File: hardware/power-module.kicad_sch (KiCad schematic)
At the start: 35 parts, among them CN1 WJ2EDGRC-5.08-2P, K1 SRD-03VDC-SL-C, K2 SRD-03VDC-SL-C, K3 SRD-03VDC-SL-C, K4 SRD-03VDC-SL-C, Q1 BC547C, Q2 BC547C, U1 MIC5205-3.3YM5-MS, U2 PM254-2-05-W-8.5, U3 CC6903SO-10A, U4 ESP32-C3-MINI-1, U5 XC6206P332MR_C5148692

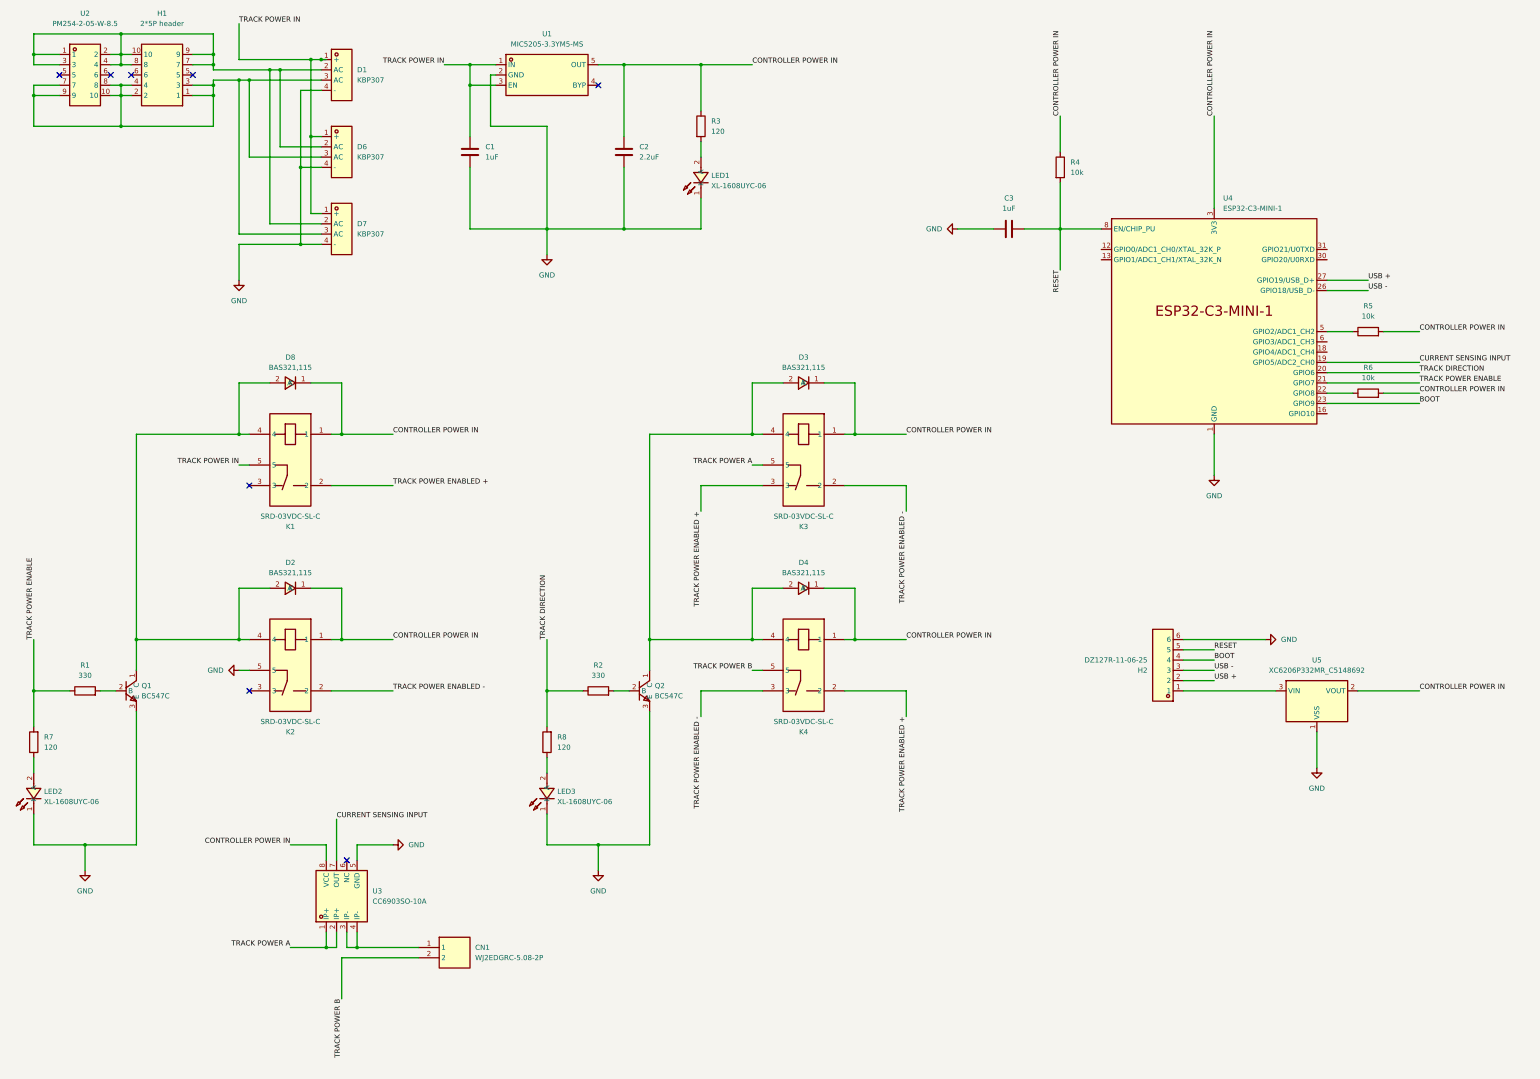
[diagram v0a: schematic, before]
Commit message: Fix relay power supply, shrinked module to 1.5 DIN module widths
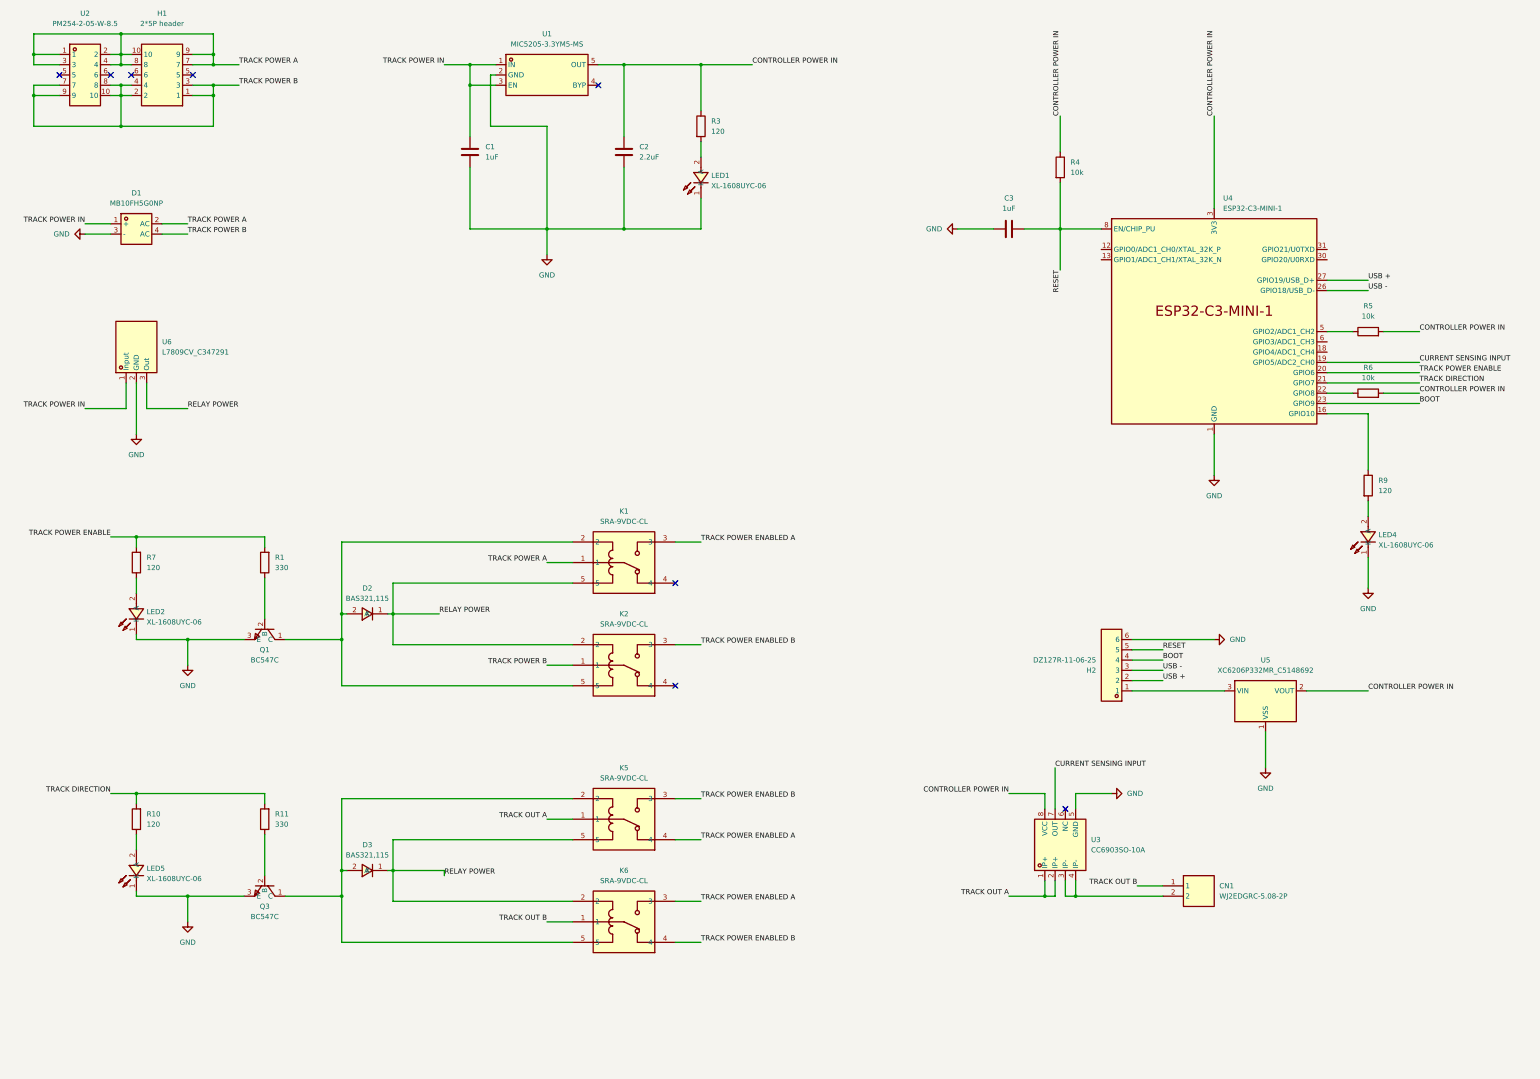
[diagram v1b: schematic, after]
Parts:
- removed D1, D6, D7: KBP307, easyeda2kicad:KBP_4P-L14.8-W3.8-P3.85-L, symbol LCSC:KBP307
- removed D4, D8: BAS321,115, easyeda2kicad:SOD-323_L1.8-W1.3-LS2.5-RD, symbol easyeda2kicad:BAS321,115
- removed K1, K2, K3, K4: SRD-03VDC-SL-C, easyeda2kicad:RELAY-TH_SRD-XXVDC-XL-C, symbol LCSC:SRD-03VDC-SL-C
- removed LED3: XL-1608UYC-06, easyeda2kicad:LED0603-RD-YELLOW, symbol easyeda2kicad:XL-1608UYC-06
- removed Q2: BC547C, easyeda2kicad:TO-92-3_L4.9-W3.7-P1.27-L, symbol LCSC:BC547C
- removed R2: 330, Resistor_SMD:R_0603_1608Metric, symbol Device:R
- removed R8: 120, Resistor_SMD:R_0603_1608Metric, symbol Device:R
- added D1: MB10FH5G0NP, LCSC:MBF_L4.8-W3.9-P2.50-LS6.7-TR, symbol LCSC:MB10FH5G0NP
- added K1, K2, K5, K6: SRA-9VDC-CL, LCSC:RELAY-TH_SRA-9VDC-CL, symbol LCSC:SRA-9VDC-CL
- added LED4, LED5: XL-1608UYC-06, LCSC:LED0603-RD-YELLOW, symbol easyeda2kicad:XL-1608UYC-06
- added Q3: BC547C, LCSC:TO-92-3_L4.9-W3.7-P1.27-L, symbol LCSC:BC547C
- added R10, R9: 120, Resistor_SMD:R_0603_1608Metric, symbol Device:R
- added R11: 330, Resistor_SMD:R_0603_1608Metric, symbol Device:R
- added U6: L7809CV_C347291, LCSC:TO-220-3_L10.0-W4.5-P2.54-L, symbol LCSC:L7809CV_C347291
- CN1: footprint easyeda2kicad:CONN-TH_2P-P5.08_WJ2EDGRC-5.08-2P -> LCSC:CONN-TH_2P-P5.08_WJ2EDGRC-5.08-2P
- D2, D3: footprint easyeda2kicad:SOD-323_L1.8-W1.3-LS2.5-RD -> LCSC:SOD-323_L1.8-W1.3-LS2.5-RD
- H1: footprint easyeda2kicad:HDR-TH_10P-P2.54-H-M-R2-C5-S2.54-W12.9 -> LCSC:HDR-TH_10P-P2.54-H-M-R2-C5-S2.54-W12.9
- H2: footprint easyeda2kicad:HDR-TH_6P-P1.27-V-M-A -> LCSC:HDR-TH_6P-P1.27-V-M-A
- LED1, LED2: footprint easyeda2kicad:LED0603-RD-YELLOW -> LCSC:LED0603-RD-YELLOW
- Q1: footprint easyeda2kicad:TO-92-3_L4.9-W3.7-P1.27-L -> LCSC:TO-92-3_L4.9-W3.7-P1.27-L
- U1: footprint easyeda2kicad:SOT-23-5_L2.9-W1.6-P0.95-LS2.8-BR -> LCSC:SOT-23-5_L2.9-W1.6-P0.95-LS2.8-BR
- U2: footprint easyeda2kicad:HDR-TH_10P-P2.54-H-F-R2-C5-W8.5 -> LCSC:HDR-TH_10P-P2.54-H-F-R2-C5-W8.5
- U3: footprint easyeda2kicad:SOP-8_L4.9-W3.9-P1.27-LS6.0-BL -> LCSC:SOP-8_L4.9-W3.9-P1.27-LS6.0-BL
- U5: footprint easyeda2kicad:SOT-23-3_L2.9-W1.3-P1.90-LS2.4-BR -> LCSC:SOT-23-3_L2.9-W1.3-P1.90-LS2.4-BR
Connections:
- net CONTROLLER POWER IN: no longer D2.1 (K), D3.1 (K)
- net GND: now also D1.3 (-), LED4.1 (K), LED5.1 (K), Q3.3 (E), U6.2 (GND)
- net TRACK DIRECTION: now also U4.21 (GPIO7), R10.2, R11.2; no longer U4.20 (GPIO6)
- net TRACK POWER A: now also H1.10, H1.7, H1.8, H1.9, U2.1, U2.2, U2.3, U2.4, D1.2 (AC), K1.1; no longer U3.1 (IP+), U3.2 (IP+)
- net TRACK POWER B: now also H1.1, H1.2, H1.3, H1.4, U2.10, U2.7, U2.8, U2.9, D1.4 (AC), K2.1; no longer CN1.2
- net TRACK POWER ENABLE: now also R1.2, U4.20 (GPIO6); no longer R1.1, U4.21 (GPIO7)
- net TRACK POWER IN: now also D1.1 (+), U6.1 (Input)
- net at D3.2 (A): now also K5.2, K6.5, Q3.1 (C)
- net at D2.2 (A), Q1.1 (C): now also K1.2, K2.5
- net at U4.16 (GPIO10): now also R9.1
- net at Q1.2 (B): now also R1.1; no longer R1.2
- net at U3.3 (IP-), U3.4 (IP-): now also CN1.2; no longer CN1.1
- new net: Q3.2 (B), R11.1
- new net: LED5.2 (A), R10.1
- new net: LED4.2 (A), R9.2
- new net RELAY POWER: D2.1 (K), D3.1 (K), K1.5, K2.2, K5.5, K6.2, U6.3 (Out)
- new net TRACK OUT A: K5.1, U3.1 (IP+), U3.2 (IP+)
- new net TRACK OUT B: CN1.1, K6.1
- new net TRACK POWER ENABLED A: K1.3, K5.4, K6.3
- new net TRACK POWER ENABLED B: K2.3, K5.3, K6.4
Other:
- moved on the sheet: H2, Q1, R7, U5

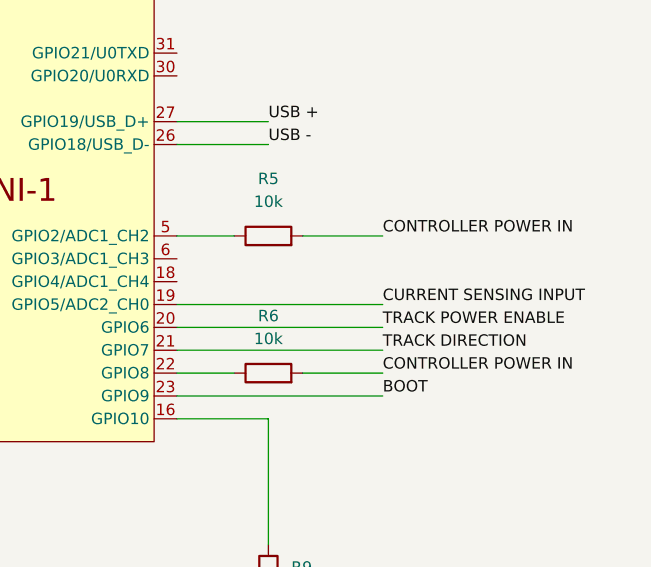
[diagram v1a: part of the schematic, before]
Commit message: Fix current sensing input on esp blocking WiFi communications
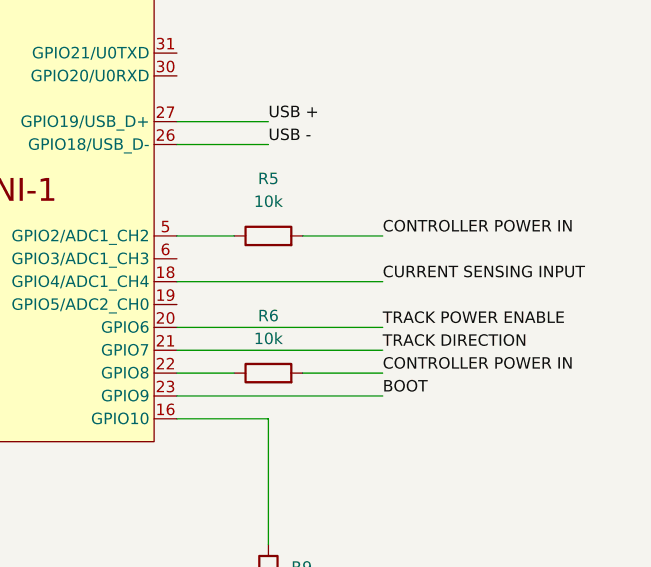
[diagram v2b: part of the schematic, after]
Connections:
- net CURRENT SENSING INPUT: now also U4.18 (GPIO4/ADC1_CH4); no longer U4.19 (GPIO5/ADC2_CH0)
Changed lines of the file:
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@@
-    (stroke (width 0) (type default))
-  )
-  (wire (pts (xy 345.44 109.22) (xy 368.3 109.22))
     (stroke (width 0) (type default))
   )
@@
     (stroke (width 0) (type default))
   )
+  (wire (pts (xy 345.44 106.68) (xy 368.3 106.68))
+    (stroke (width 0) (type default))
+  )
   (wire (pts (xy 69.85 35.56) (xy 76.2 35.56))
     (stroke (width 0) (type default))
@@
     (effects (font (size 1.27 1.27)) (justify left bottom))
   )
-  (label "CURRENT SENSING INPUT" (at 368.3 109.22 0) (fields_autoplaced)
-    (effects (font (size 1.27 1.27)) (justify left bottom))
-  )
   (label "CONTROLLER POWER IN" (at 279.4 48.26 90) (fields_autoplaced)
     (effects (font (size 1.27 1.27)) (justify left bottom))
@@
     (effects (font (size 1.27 1.27)) (justify left bottom))
   )
+  (label "CURRENT SENSING INPUT" (at 368.3 106.68 0) (fields_autoplaced)
+    (effects (font (size 1.27 1.27)) (justify left bottom))
+  )

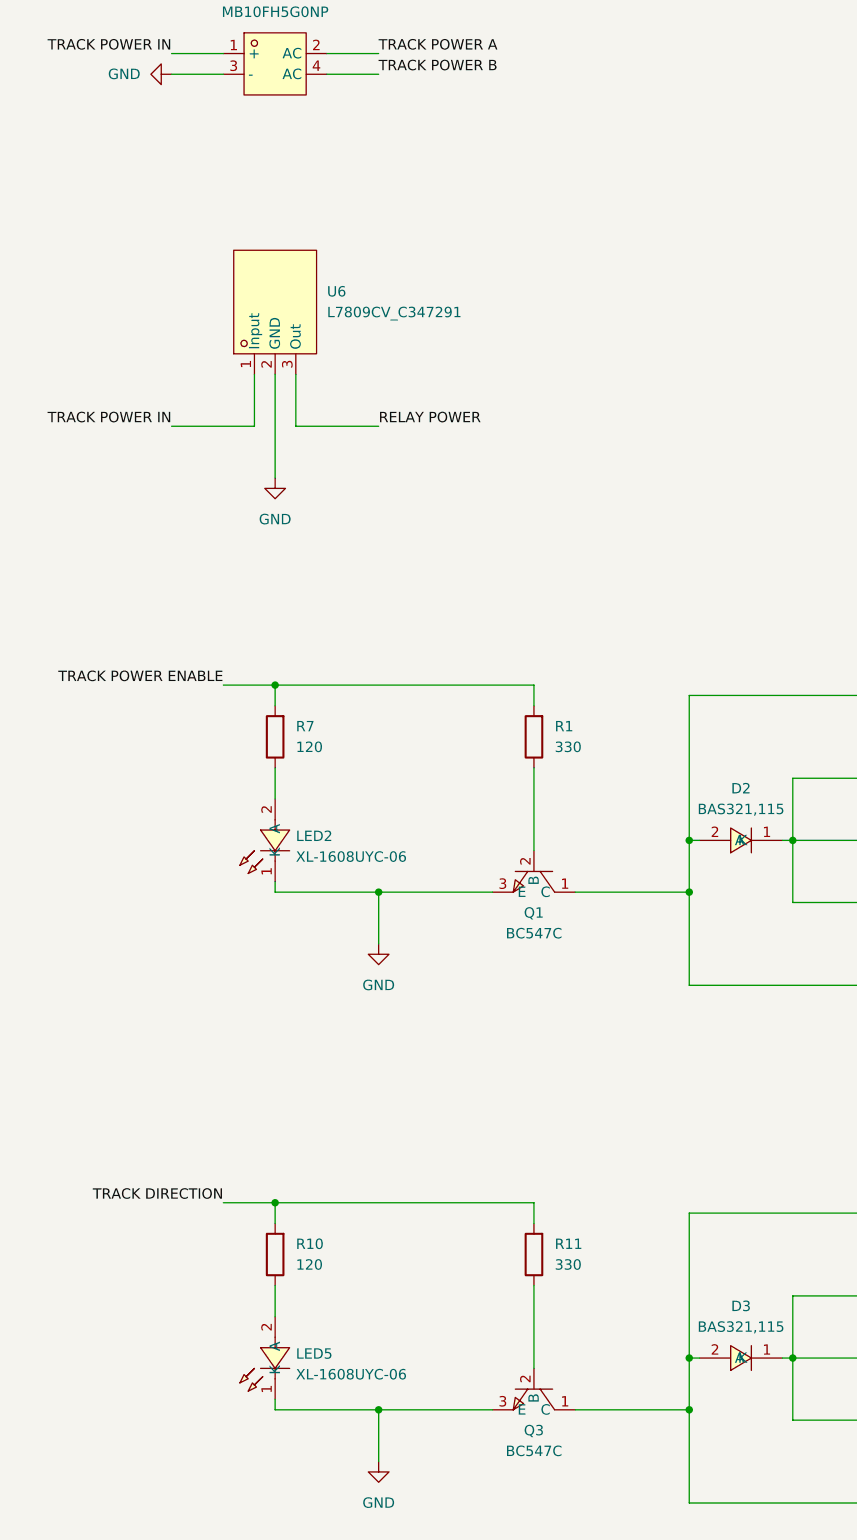
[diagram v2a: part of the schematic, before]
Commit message: Fix relay switching transistors current rating
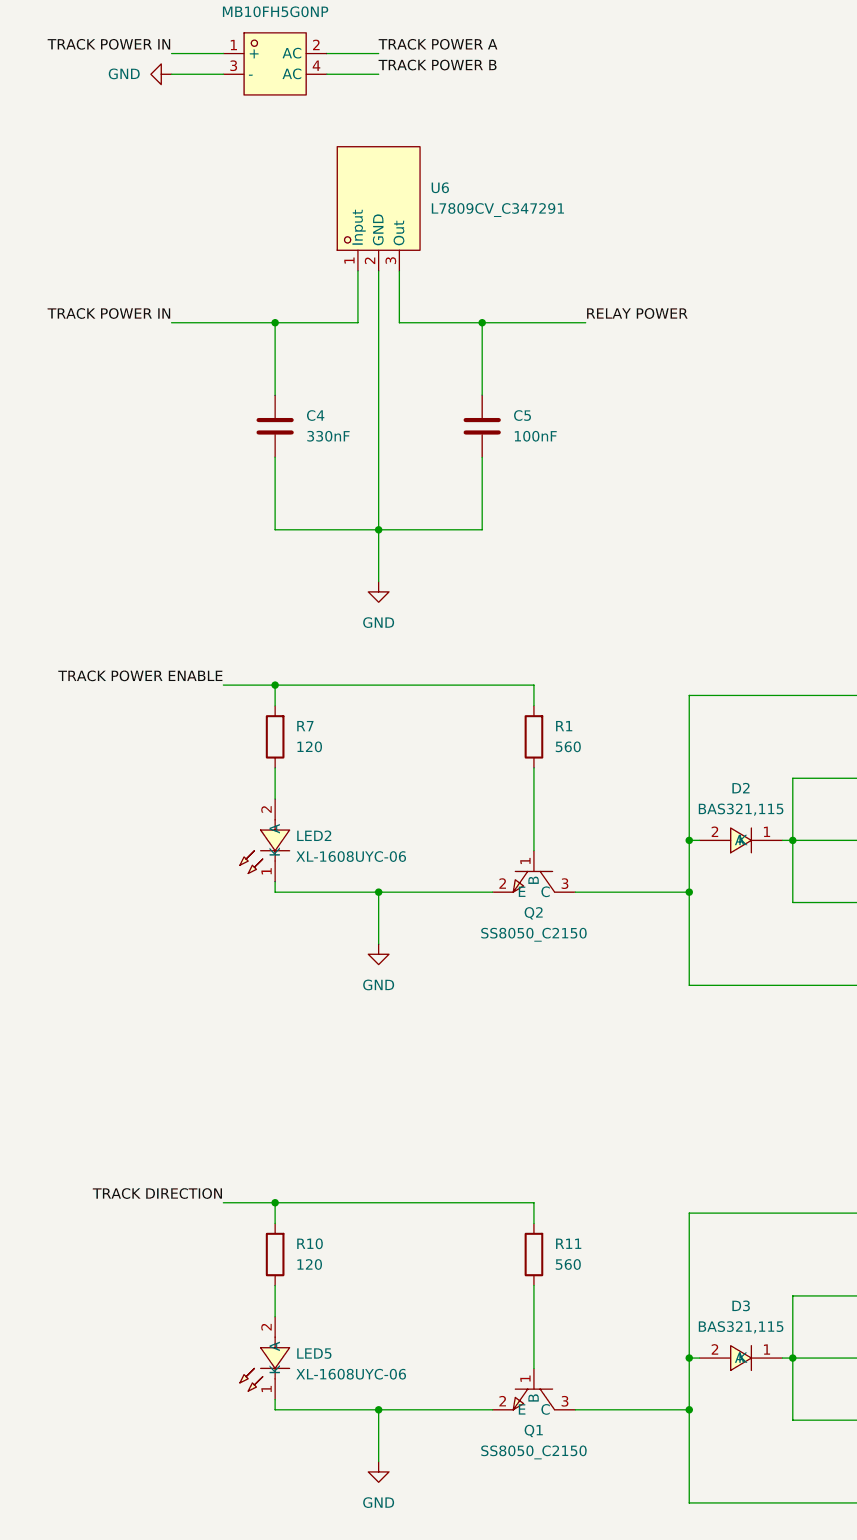
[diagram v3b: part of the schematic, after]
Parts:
- removed Q1, Q3: BC547C, LCSC:TO-92-3_L4.9-W3.7-P1.27-L, symbol LCSC:BC547C
- added C4: 330nF, Capacitor_SMD:C_0603_1608Metric, symbol Device:C
- added C5: 100nF, Capacitor_SMD:C_0603_1608Metric, symbol Device:C
- added Q1, Q2: SS8050_C2150, LCSC:SOT-23-3_L2.9-W1.3-P1.90-LS2.4-BR, symbol LCSC:SS8050_C2150
- R1, R11: value 330 -> 560
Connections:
- net GND: now also C4.2, C5.2, Q1.2 (E), Q2.2 (E)
- net RELAY POWER: now also C5.1
- net TRACK POWER IN: now also C4.1
- net at D3.2 (A), K5.2, K6.5: now also Q1.3 (C)
- net at R11.1: now also Q1.1 (B)
- net at D2.2 (A), K1.2, K2.5: now also Q2.3 (C)
- net at R1.1: now also Q2.1 (B)
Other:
- moved on the sheet: U6
